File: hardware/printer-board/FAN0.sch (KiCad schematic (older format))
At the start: 8 parts, among them J38 TO FAN0, Q4 D882

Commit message: update,
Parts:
- Q4: footprint Package_TO_SOT_SMD:SOT-89-3 -> footprint-lib:SOT-89-3,thermal_vias
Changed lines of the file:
@@
 F 0 "Q4" H 3350 3700 50  0000 L CNN
 F 1 "D882" H 3350 3650 50  0000 L CNN
-F 2 "Package_TO_SOT_SMD:SOT-89-3" H 3350 3750 50  0001 C CNN
+F 2 "footprint-lib:SOT-89-3,thermal_vias" H 3350 3750 50  0001 C CNN
 F 3 "" H 3150 3650 50  0001 C CNN
 	1    3150 3650

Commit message: update to re-annotation,
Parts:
- renumbered C33 to C36, D10 to D20, J38 to J33, R42 to R56, R44 to R57, R36 to R58, R43 to R59
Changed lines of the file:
@@
 AR Path="/5CC130A8/5CC242F9" Ref="J?"  Part="1"
 AR Path="/5CC19D48/5CC242F9" Ref="J?"  Part="1"
-AR Path="/5CC2401E/5CC242A1/5CC242F9" Ref="J38"  Part="1"
+AR Path="/5CC2401E/5CC242A1/5CC242F9" Ref="J33"  Part="1"
 AR Path="/5CC2401E/5CC24321/5CC242F9" Ref="J?"  Part="1"
-AR Path="/5CC242F9" Ref="J38"  Part="1"
-F 0 "J38" H 4300 2550 50  0000 C CNN
+AR Path="/5CC242F9" Ref="J?"  Part="1"
+F 0 "J33" H 4300 2550 50  0000 C CNN
 F 1 "TO FAN0" H 4300 2650 50  0000 C CNN
 F 2 "footprint-lib:b2b-ph-kl,fan_pwm_out" H 4350 2900 50  0001 C CNN
@@
 AR Path="/5CC130A8/5CC8A042" Ref="R?"  Part="1"
 AR Path="/5CC19D48/5CC8A042" Ref="R?"  Part="1"
-AR Path="/5CC2401E/5CC242A1/5CC8A042" Ref="R42"  Part="1"
+AR Path="/5CC2401E/5CC242A1/5CC8A042" Ref="R56"  Part="1"
 AR Path="/5CC2401E/5CC24321/5CC8A042" Ref="R?"  Part="1"
-AR Path="/5CC8A042" Ref="R42"  Part="1"
-F 0 "R42" V 2304 3650 50  0000 C CNN
+AR Path="/5CC8A042" Ref="R?"  Part="1"
+F 0 "R56" V 2304 3650 50  0000 C CNN
 F 1 "R100,0805" V 2395 3650 50  0000 C CNN
 F 2 "Resistor_SMD:R_0805_2012Metric_Pad1.15x1.40mm_HandSolder" H 2500 3650 50  0001 C CNN
@@
 AR Path="/5CC130A8/5CC8A033" Ref="R?"  Part="1"
 AR Path="/5CC19D48/5CC8A033" Ref="R?"  Part="1"
-AR Path="/5CC2401E/5CC242A1/5CC8A033" Ref="R44"  Part="1"
+AR Path="/5CC2401E/5CC242A1/5CC8A033" Ref="R57"  Part="1"
 AR Path="/5CC2401E/5CC24321/5CC8A033" Ref="R?"  Part="1"
-AR Path="/5CC8A033" Ref="R44"  Part="1"
-F 0 "R44" V 2304 4050 50  0000 C CNN
+AR Path="/5CC8A033" Ref="R?"  Part="1"
+F 0 "R57" V 2304 4050 50  0000 C CNN
 F 1 "R104,0805" V 2395 4050 50  0000 C CNN
 F 2 "Resistor_SMD:R_0805_2012Metric_Pad1.15x1.40mm_HandSolder" H 2500 4050 50  0001 C CNN
@@
 AR Path="/5CC130A8/5CC242FE" Ref="#PWR?"  Part="1"
 AR Path="/5CC19D48/5CC242FE" Ref="#PWR?"  Part="1"
-AR Path="/5CC2401E/5CC242A1/5CC242FE" Ref="#PWR0258"  Part="1"
+AR Path="/5CC2401E/5CC242A1/5CC242FE" Ref="#PWR0162"  Part="1"
 AR Path="/5CC2401E/5CC24321/5CC242FE" Ref="#PWR?"  Part="1"
-AR Path="/5CC242FE" Ref="#PWR0258"  Part="1"
-F 0 "#PWR0258" H 3250 4000 50  0001 C CNN
+AR Path="/5CC242FE" Ref="#PWR?"  Part="1"
+F 0 "#PWR0162" H 3250 4000 50  0001 C CNN
 F 1 "GND" H 3255 4077 50  0000 C CNN
 F 2 "" H 3250 4250 50  0001 C CNN
@@
 AR Path="/5CC130A8/5CC8A037" Ref="R?"  Part="1"
 AR Path="/5CC19D48/5CC8A037" Ref="R?"  Part="1"
-AR Path="/5CC2401E/5CC242A1/5CC8A037" Ref="R43"  Part="1"
+AR Path="/5CC2401E/5CC242A1/5CC8A037" Ref="R59"  Part="1"
 AR Path="/5CC2401E/5CC24321/5CC8A037" Ref="R?"  Part="1"
-AR Path="/5CC8A037" Ref="R43"  Part="1"
-F 0 "R43" H 3809 2546 50  0000 L CNN
+AR Path="/5CC8A037" Ref="R?"  Part="1"
+F 0 "R59" H 3809 2546 50  0000 L CNN
 F 1 "R182,0603" H 3809 2455 50  0000 L CNN
 F 2 "Resistor_SMD:R_0603_1608Metric_Pad1.05x0.95mm_HandSolder" H 3750 2500 50  0001 C CNN
@@
 AR Path="/5CC130A8/5CC242FF" Ref="#PWR?"  Part="1"
 AR Path="/5CC19D48/5CC242FF" Ref="#PWR?"  Part="1"
-AR Path="/5CC2401E/5CC242A1/5CC242FF" Ref="#PWR0259"  Part="1"
+AR Path="/5CC2401E/5CC242A1/5CC242FF" Ref="#PWR0163"  Part="1"
 AR Path="/5CC2401E/5CC24321/5CC242FF" Ref="#PWR?"  Part="1"
-AR Path="/5CC242FF" Ref="#PWR0259"  Part="1"
-F 0 "#PWR0259" H 4000 2050 50  0001 C CNN
+AR Path="/5CC242FF" Ref="#PWR?"  Part="1"
+F 0 "#PWR0163" H 4000 2050 50  0001 C CNN
 F 1 "+12V" H 4015 2373 50  0000 C CNN
 F 2 "" H 4000 2200 50  0001 C CNN
@@
 AR Path="/5CC130A8/5CC8A044" Ref="D?"  Part="1"
 AR Path="/5CC19D48/5CC8A044" Ref="D?"  Part="1"
-AR Path="/5CC2401E/5CC242A1/5CC8A044" Ref="D10"  Part="1"
+AR Path="/5CC2401E/5CC242A1/5CC8A044" Ref="D20"  Part="1"
 AR Path="/5CC2401E/5CC24321/5CC8A044" Ref="D?"  Part="1"
-AR Path="/5CC8A044" Ref="D10"  Part="1"
-F 0 "D10" V 3704 2898 50  0000 L CNN
+AR Path="/5CC8A044" Ref="D?"  Part="1"
+F 0 "D20" V 3704 2898 50  0000 L CNN
 F 1 "LED_BLUE,0603" V 3795 2898 50  0000 L CNN
 F 2 "LED_SMD:LED_0603_1608Metric_Pad1.05x0.95mm_HandSolder" V 3750 2800 50  0001 C CNN
@@
 AR Path="/5CC130A8/5CC24301" Ref="#PWR?"  Part="1"
 AR Path="/5CC19D48/5CC24301" Ref="#PWR?"  Part="1"
-AR Path="/5CC2401E/5CC242A1/5CC24301" Ref="#PWR0260"  Part="1"
+AR Path="/5CC2401E/5CC242A1/5CC24301" Ref="#PWR0160"  Part="1"
 AR Path="/5CC2401E/5CC24321/5CC24301" Ref="#PWR?"  Part="1"
-AR Path="/5CC24301" Ref="#PWR0260"  Part="1"
-F 0 "#PWR0260" H 2600 4600 50  0001 C CNN
+AR Path="/5CC24301" Ref="#PWR?"  Part="1"
+F 0 "#PWR0160" H 2600 4600 50  0001 C CNN
 F 1 "+12V" V 2615 4878 50  0000 L CNN
 F 2 "" H 2600 4750 50  0001 C CNN
@@
 AR Path="/5CC130A8/5CC24302" Ref="#PWR?"  Part="1"
 AR Path="/5CC19D48/5CC24302" Ref="#PWR?"  Part="1"
-AR Path="/5CC2401E/5CC242A1/5CC24302" Ref="#PWR0261"  Part="1"
+AR Path="/5CC2401E/5CC242A1/5CC24302" Ref="#PWR0161"  Part="1"
 AR Path="/5CC2401E/5CC24321/5CC24302" Ref="#PWR?"  Part="1"
-AR Path="/5CC24302" Ref="#PWR0261"  Part="1"
-F 0 "#PWR0261" H 3100 4500 50  0001 C CNN
+AR Path="/5CC24302" Ref="#PWR?"  Part="1"
+F 0 "#PWR0161" H 3100 4500 50  0001 C CNN
 F 1 "GND" H 3105 4577 50  0000 C CNN
 F 2 "" H 3100 4750 50  0001 C CNN
@@
 AR Path="/5CC12903/5CC8A040" Ref="C?"  Part="1"
 AR Path="/5CC19D48/5CC8A040" Ref="C?"  Part="1"
-AR Path="/5CC2401E/5CC242A1/5CC8A040" Ref="C33"  Part="1"
+AR Path="/5CC2401E/5CC242A1/5CC8A040" Ref="C36"  Part="1"
 AR Path="/5CC2401E/5CC24321/5CC8A040" Ref="C?"  Part="1"
-AR Path="/5CC8A040" Ref="C33"  Part="1"
-F 0 "C33" V 3075 4750 50  0000 C CNN
+AR Path="/5CC8A040" Ref="C?"  Part="1"
+F 0 "C36" V 3075 4750 50  0000 C CNN
 F 1 "CP100uf,16V" V 2984 4750 50  0000 C CNN
 F 2 "Capacitor_SMD:CP_Elec_6.3x5.3" H 2850 4750 50  0001 C CNN
@@
 $EndComp
 $Comp
-L taobao-r:R100,0603 R36
+L taobao-r:R100,0603 R58
 U 1 1 5CC8A048
 P 3250 3150
-F 0 "R36" H 3350 3200 50  0000 L CNN
+F 0 "R58" H 3350 3200 50  0000 L CNN
 F 1 "R100,0603" H 3350 3150 50  0000 L CNN
 F 2 "Resistor_SMD:R_0603_1608Metric_Pad1.05x0.95mm_HandSolder" H 3250 3150 50  0001 C CNN

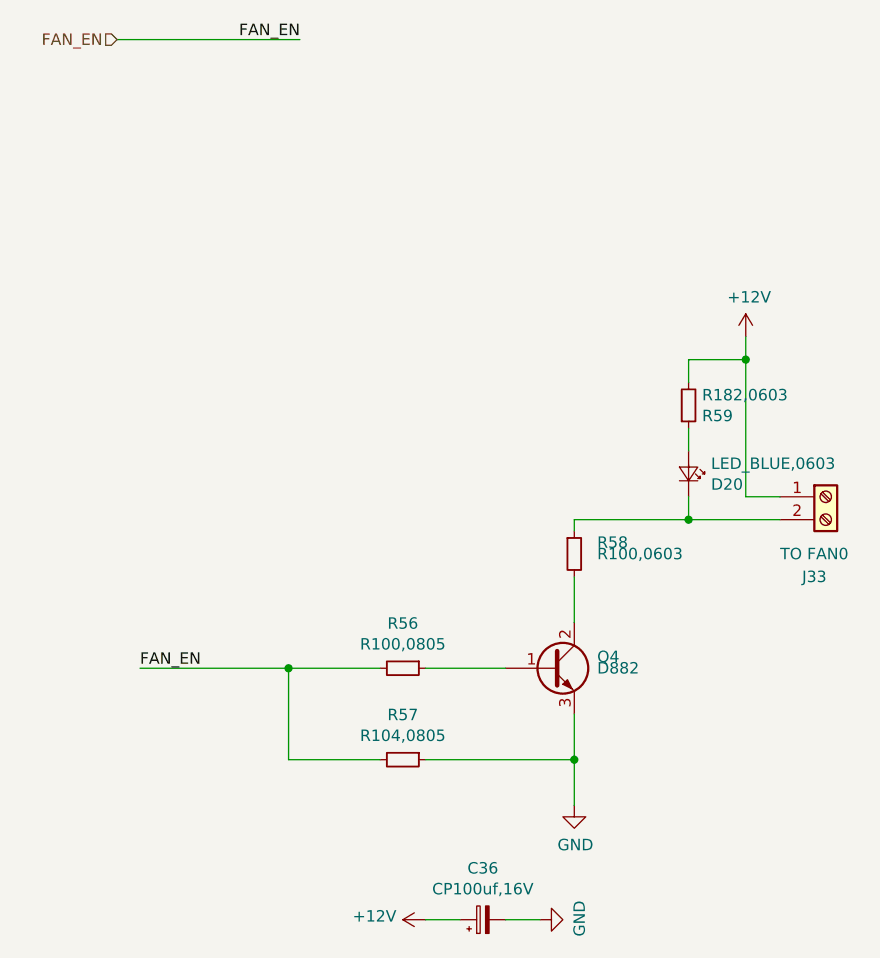
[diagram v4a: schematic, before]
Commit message: update step motor terminal orientation,
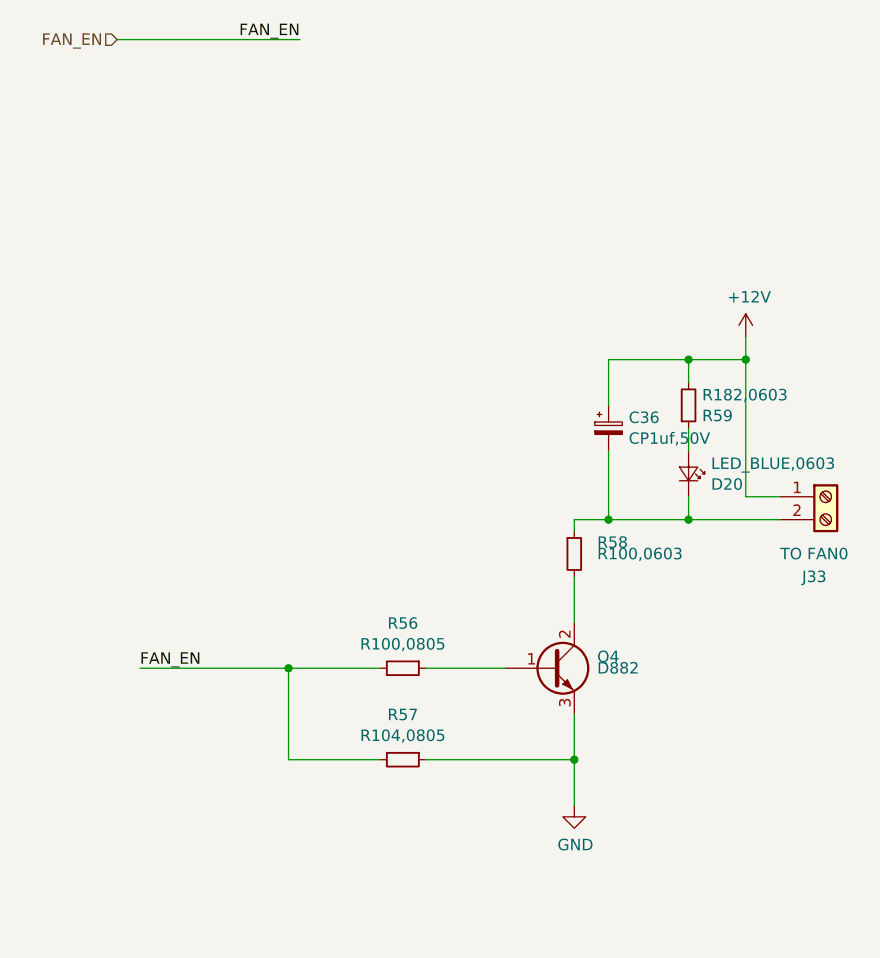
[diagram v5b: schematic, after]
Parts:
- removed C36: CP100uf,16V, Capacitor_SMD:CP_Elec_6.3x5.3, symbol taobao-cp:CP100uf,16V
- added C36: CP1uf,50V, Capacitor_SMD:CP_Elec_4x5.3, symbol taobao-cp:CP1uf,50V
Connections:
- net +12V: now also C36.1
- net at D20.1 (K), J33.2 (Pin_2), R58.1: now also C36.2
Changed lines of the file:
@@
 $Descr A4 11693 8268
 encoding utf-8
-Sheet 1 29
+Sheet 22 29
 Title ""
 Date ""
@@
 	0    1    -1   0
 $EndComp
-$Comp
-L power:+12V #PWR?
-U 1 1 5CC24301
-P 2600 4750
-AR Path="/5CC12903/5CC24301" Ref="#PWR?"  Part="1"
-AR Path="/5CC130A8/5CC24301" Ref="#PWR?"  Part="1"
-AR Path="/5CC19D48/5CC24301" Ref="#PWR?"  Part="1"
-AR Path="/5CC2401E/5CC242A1/5CC24301" Ref="#PWR0160"  Part="1"
-AR Path="/5CC2401E/5CC24321/5CC24301" Ref="#PWR?"  Part="1"
-AR Path="/5CC24301" Ref="#PWR0160"  Part="1"
-F 0 "#PWR0160" H 2600 4600 50  0001 C CNN
-F 1 "+12V" V 2615 4878 50  0000 L CNN
-F 2 "" H 2600 4750 50  0001 C CNN
-F 3 "" H 2600 4750 50  0001 C CNN
-	1    2600 4750
-	0    -1   -1   0
-$EndComp
-$Comp
-L power:GND #PWR?
-U 1 1 5CC24302
-P 3100 4750
-AR Path="/5CC0B758/5CC24302" Ref="#PWR?"  Part="1"
-AR Path="/5CC12903/5CC24302" Ref="#PWR?"  Part="1"
-AR Path="/5CC130A8/5CC24302" Ref="#PWR?"  Part="1"
-AR Path="/5CC19D48/5CC24302" Ref="#PWR?"  Part="1"
-AR Path="/5CC2401E/5CC242A1/5CC24302" Ref="#PWR0161"  Part="1"
-AR Path="/5CC2401E/5CC24321/5CC24302" Ref="#PWR?"  Part="1"
-AR Path="/5CC24302" Ref="#PWR0161"  Part="1"
-F 0 "#PWR0161" H 3100 4500 50  0001 C CNN
-F 1 "GND" H 3105 4577 50  0000 C CNN
-F 2 "" H 3100 4750 50  0001 C CNN
-F 3 "" H 3100 4750 50  0001 C CNN
-	1    3100 4750
-	0    -1   -1   0
-$EndComp
-$Comp
-L taobao-cp:CP100uf,16V C?
-U 1 1 5CC8A040
-P 2850 4750
-AR Path="/5CC12903/5CC8A040" Ref="C?"  Part="1"
-AR Path="/5CC19D48/5CC8A040" Ref="C?"  Part="1"
-AR Path="/5CC2401E/5CC242A1/5CC8A040" Ref="C36"  Part="1"
-AR Path="/5CC2401E/5CC24321/5CC8A040" Ref="C?"  Part="1"
-AR Path="/5CC8A040" Ref="C36"  Part="1"
-F 0 "C36" V 3075 4750 50  0000 C CNN
-F 1 "CP100uf,16V" V 2984 4750 50  0000 C CNN
-F 2 "Capacitor_SMD:CP_Elec_6.3x5.3" H 2850 4750 50  0001 C CNN
-F 3 "~" H 2850 4750 50  0001 C CNN
-	1    2850 4750
-	0    -1   -1   0
-$EndComp
-Wire Wire Line
-	2600 4750 2750 4750
-Wire Wire Line
-	2950 4750 3100 4750
 $Bitmap
 Pos 9550 5050
@@
 	4000 2200 4000 2300
 Wire Wire Line
-	3250 3000 3750 3000
+	3250 3000 3400 3000
 Wire Wire Line
 	3250 3000 3250 3050
@@
 	4000 2300 4000 2900
 Connection ~ 4000 2300
+$Comp
+L taobao-cp:CP1uf,50V C36
+U 1 1 5CCC20EB
+P 3400 2600
+F 0 "C36" H 3488 2646 50  0000 L CNN
+F 1 "CP1uf,50V" H 3488 2555 50  0000 L CNN
+F 2 "Capacitor_SMD:CP_Elec_4x5.3" H 3400 2600 50  0001 C CNN
+F 3 "~" H 3400 2600 50  0001 C CNN
+	1    3400 2600
+	1    0    0    -1
+$EndComp
+Wire Wire Line
+	3750 2300 3400 2300
+Wire Wire Line
+	3400 2300 3400 2500
+Connection ~ 3750 2300
+Wire Wire Line
+	3400 2700 3400 3000
+Connection ~ 3400 3000
+Wire Wire Line
+	3400 3000 3750 3000
 $EndSCHEMATC

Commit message: update ROUTING,
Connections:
- net FAN_EN renamed FAN0_EN
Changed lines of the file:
@@
 $Descr A4 11693 8268
 encoding utf-8
-Sheet 22 27
+Sheet 20 28
 Title ""
 Date ""
@@
 AR Path="/5CC2401E/5CC24321/5CC242F9" Ref="J?"  Part="1"
 AR Path="/5CC242F9" Ref="J33"  Part="1"
+AR Path="/5CC2401E/5CE37797/5CC242F9" Ref="J?"  Part="1"
 F 0 "J33" H 4300 2550 50  0000 C CNN
 F 1 "TO FAN0" H 4300 2650 50  0000 C CNN
@@
 AR Path="/5CC2401E/5CC24321/5CC8A042" Ref="R?"  Part="1"
 AR Path="/5CC8A042" Ref="R56"  Part="1"
+AR Path="/5CC2401E/5CE37797/5CC8A042" Ref="R?"  Part="1"
 F 0 "R56" V 2304 3650 50  0000 C CNN
 F 1 "R100,0805" V 2395 3650 50  0000 C CNN
@@
 AR Path="/5CC2401E/5CC24321/5CC8A033" Ref="R?"  Part="1"
 AR Path="/5CC8A033" Ref="R57"  Part="1"
+AR Path="/5CC2401E/5CE37797/5CC8A033" Ref="R?"  Part="1"
 F 0 "R57" V 2304 4050 50  0000 C CNN
 F 1 "R104,0805" V 2395 4050 50  0000 C CNN
@@
 AR Path="/5CC2401E/5CC24321/5CC242FE" Ref="#PWR?"  Part="1"
 AR Path="/5CC242FE" Ref="#PWR0162"  Part="1"
+AR Path="/5CC2401E/5CE37797/5CC242FE" Ref="#PWR?"  Part="1"
 F 0 "#PWR0162" H 3250 4000 50  0001 C CNN
 F 1 "GND" H 3255 4077 50  0000 C CNN
@@
 AR Path="/5CC2401E/5CC24321/5CC8A037" Ref="R?"  Part="1"
 AR Path="/5CC8A037" Ref="R59"  Part="1"
+AR Path="/5CC2401E/5CE37797/5CC8A037" Ref="R?"  Part="1"
 F 0 "R59" H 3809 2546 50  0000 L CNN
 F 1 "R182,0603" H 3809 2455 50  0000 L CNN
@@
 	4150 2900 4000 2900
 Text HLabel 1250 900  0    50   Input ~ 0
-FAN_EN
+FAN0_EN
 Text Label 2050 900  2    50   ~ 0
-FAN_EN
+FAN0_EN
 Wire Wire Line
 	1250 900  2050 900
 Text Label 1350 3650 0    50   ~ 0
-FAN_EN
+FAN0_EN
 Wire Wire Line
 	1350 3650 2000 3650
@@
 AR Path="/5CC2401E/5CC24321/5CC242FF" Ref="#PWR?"  Part="1"
 AR Path="/5CC242FF" Ref="#PWR0163"  Part="1"
+AR Path="/5CC2401E/5CE37797/5CC242FF" Ref="#PWR?"  Part="1"
 F 0 "#PWR0163" H 4000 2050 50  0001 C CNN
 F 1 "+12V" H 4015 2373 50  0000 C CNN
@@
 AR Path="/5CC2401E/5CC24321/5CC8A044" Ref="D?"  Part="1"
 AR Path="/5CC8A044" Ref="D20"  Part="1"
+AR Path="/5CC2401E/5CE37797/5CC8A044" Ref="D?"  Part="1"
 F 0 "D20" V 3704 2898 50  0000 L CNN
 F 1 "LED_BLUE,0603" V 3795 2898 50  0000 L CNN
@@
 U 1 1 5CC87678
 P 3150 3650
+AR Path="/5CC2401E/5CC242A1/5CC87678" Ref="Q4"  Part="1"
+AR Path="/5CC2401E/5CE37797/5CC87678" Ref="Q?"  Part="1"
 F 0 "Q4" H 3350 3700 50  0000 L CNN
 F 1 "D882" H 3350 3650 50  0000 L CNN
@@
 U 1 1 5CC8A048
 P 3250 3150
+AR Path="/5CC2401E/5CC242A1/5CC8A048" Ref="R58"  Part="1"
+AR Path="/5CC2401E/5CE37797/5CC8A048" Ref="R?"  Part="1"
 F 0 "R58" H 3350 3200 50  0000 L CNN
 F 1 "R100,0603" H 3350 3150 50  0000 L CNN
@@
 U 1 1 5CCC20EB
 P 3400 2600
+AR Path="/5CC2401E/5CC242A1/5CCC20EB" Ref="C36"  Part="1"
+AR Path="/5CC2401E/5CE37797/5CCC20EB" Ref="C?"  Part="1"
 F 0 "C36" H 3488 2646 50  0000 L CNN
 F 1 "CP1uf,50V" H 3488 2555 50  0000 L CNN
